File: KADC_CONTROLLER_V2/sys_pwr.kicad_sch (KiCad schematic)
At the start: 57 parts, among them J3 PJ-202AH, J6 22112022, Q1 DMN2310U-7, Q2 DMN2310U-7, U26 CSD18532Q5B, U27 MP8772GQ-Z, U28 MP8904DD-LF-Z, U29 MMSD4148T1G, U6 MP5016HGQH-Z

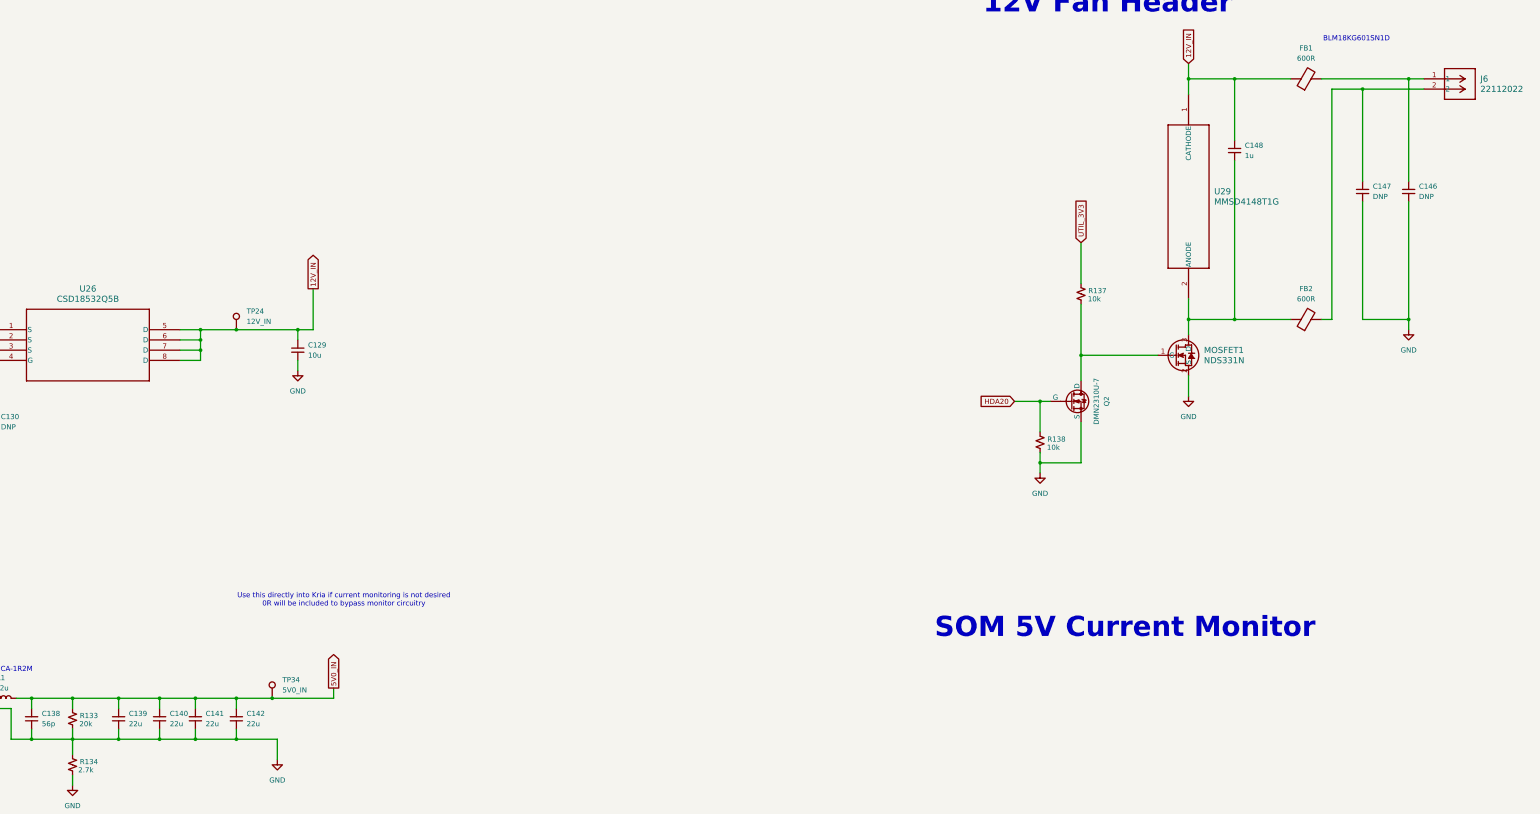
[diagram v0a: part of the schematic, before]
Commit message: Added footprints, updated schematic
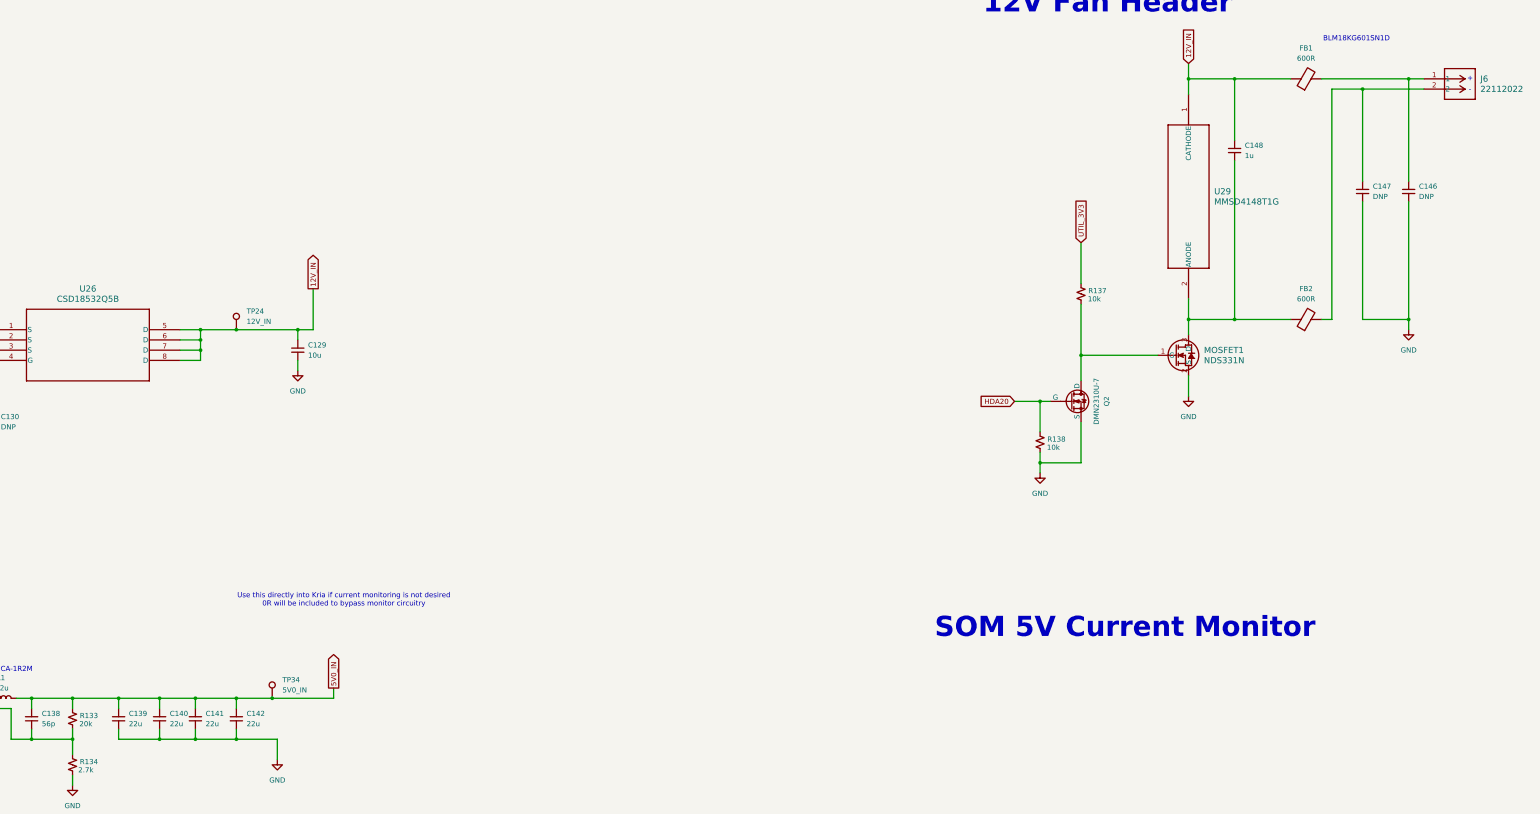
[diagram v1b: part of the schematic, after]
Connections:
- net GND: no longer C138.1, R132.1, R133.2, R134.1
- new net: C138.1, R132.1, R133.2, R134.1
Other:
- note added: "+"
- note added: "-"
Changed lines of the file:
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@@
 	(generator_version "10.0")
 	(paper "A2")
+	(text "-"
+		(exclude_from_sim no)
+		(at 558.8 47.244 0)
+		(effects
+			(font
+				(size 1.27 1.27)
+			)
+		)
+	)
 	(text "12V Plug"
 		(exclude_from_sim no)
@@
 		)
 	)
+	(text "+"
+		(exclude_from_sim no)
+		(at 558.8 44.45 0)
+		(effects
+			(font
+				(size 1.27 1.27)
+			)
+		)
+	)
 	(text "3.3 Auxiliary Regulator"
 		(exclude_from_sim no)
@@
 	)
 	(junction
-		(at 223.52 208.28)
-		(diameter 0)
-		(color 0 0 0 0)
-	)
-	(junction
 		(at 488.95 104.14)
 		(diameter 0)
@@
 		)
 		(stroke
-			(width 0)
-			(type default)
-		)
-	)
-	(wire
-		(pts
-			(xy 212.09 208.28) (xy 223.52 208.28)
-		)
-		(stroke

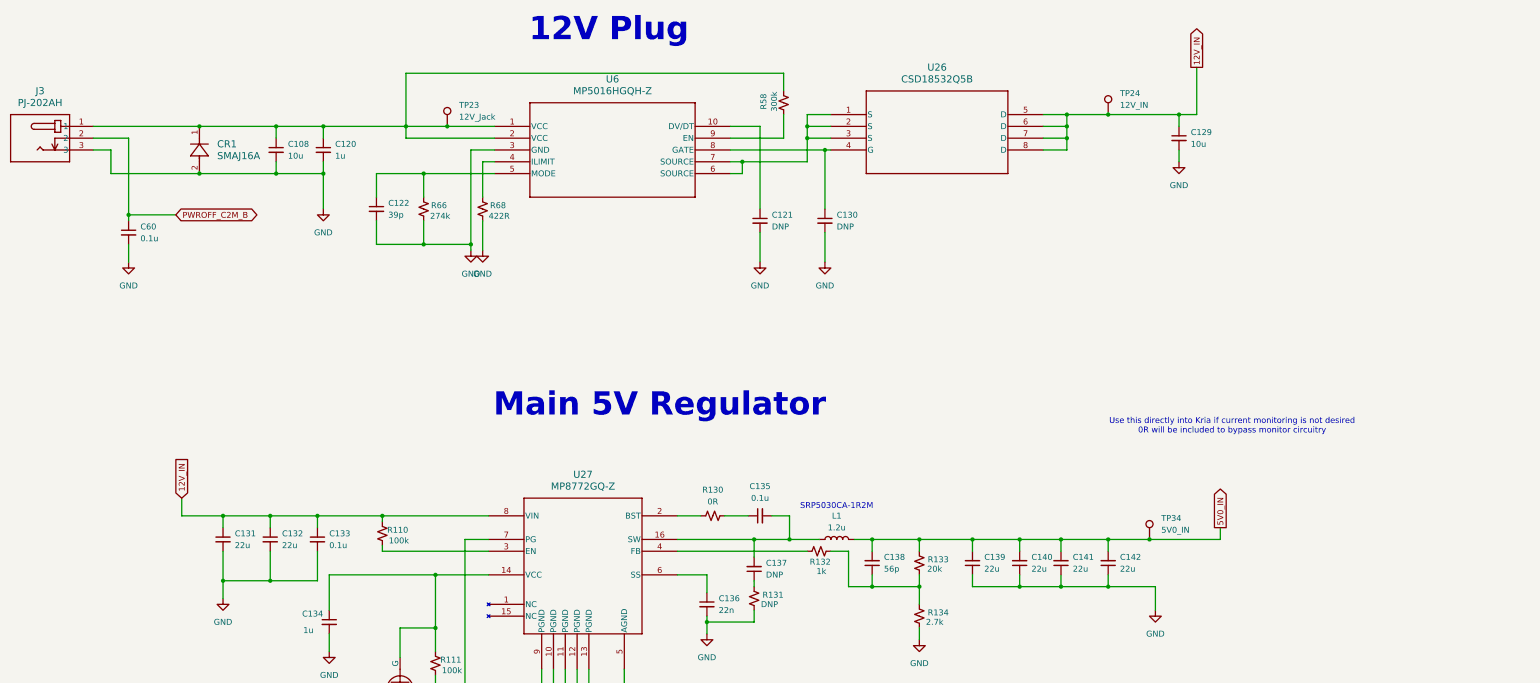
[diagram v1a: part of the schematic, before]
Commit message: Added SOM dedicated power rail
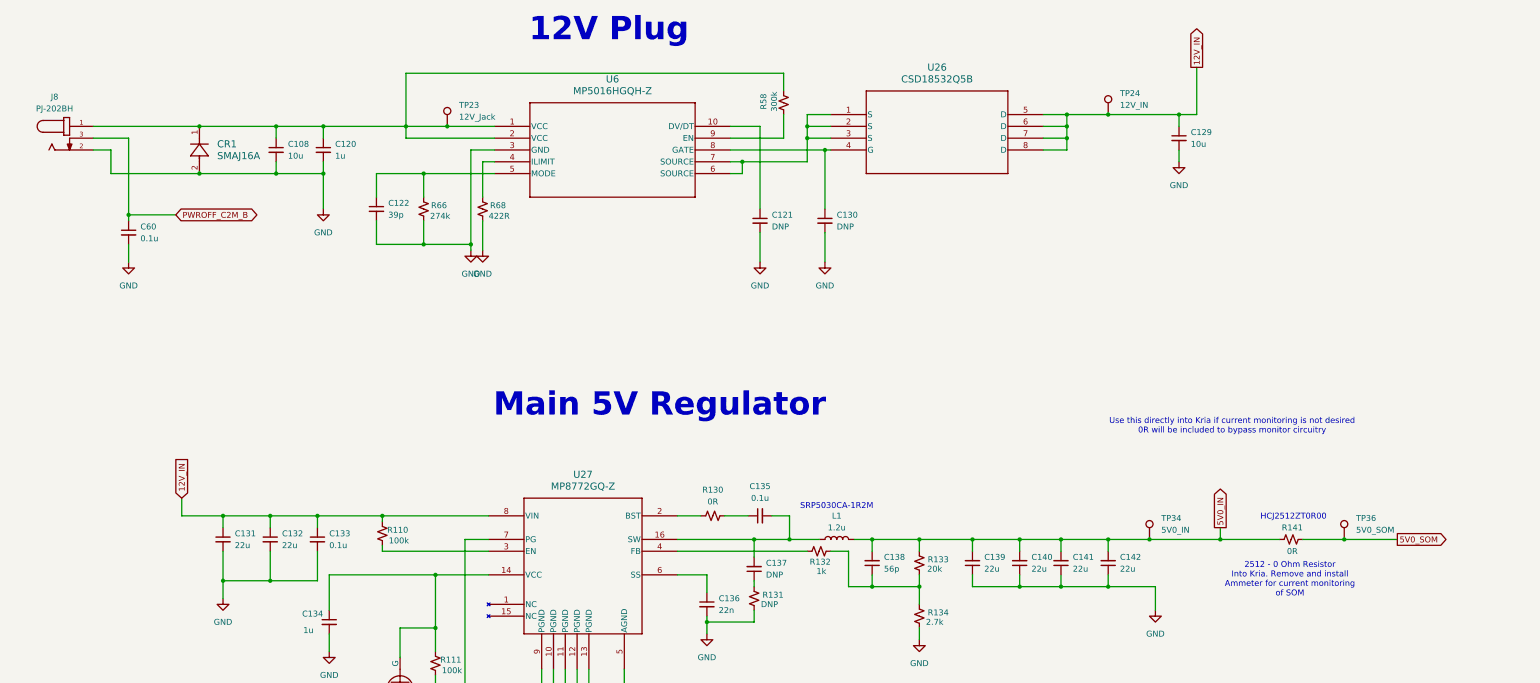
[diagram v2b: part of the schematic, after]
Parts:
- removed J3: PJ-202AH, CONN3_PJ-202_CUD, symbol PJ_202AH:PJ-202AH
- added J8: PJ-202BH, PJ-202BH:CUI_PJ-202BH, symbol PJ-202BH:PJ-202BH
- added R141: 0R, HCJ2512ZT0R00:RES_HCJ2512_STP, symbol Device:R_Small_US
- added TP36: 5V0_SOM, TestPoint:TestPoint_THTPad_1.5x1.5mm_Drill0.7mm, symbol Connector:TestPoint
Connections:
- net 5V0_IN: now also R141.1
- net GND: now also J8.2
- net PWROFF_C2M_B: now also J8.3
- net at C108.1, C120.1, CR1.1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: now also J8.1
- new net 5V0_SOM: R141.2, TP36.1
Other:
- note added: "2512 - 0 Ohm Resistor Into Kria. Remove and install Ammeter for current monitoring of SOM"
- note added: "HCJ2512ZT0R00"

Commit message: Updated Transistors
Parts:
- removed Q1: DMN2310U-7, Package_TO_SOT_SMD:TSOT-23, symbol Simulation_SPICE:NMOS
- added Q12: BSS806NEH6327XTSA1, Package_TO_SOT_SMD:SOT-23-3, symbol Transistor_FET:Q_NMOS_GSD
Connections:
- net PWROFF_C2M_B: now also Q12.3 (D)
- net at C134.1, R111.2, U27.14 (VCC): now also Q12.1 (G)
- net at R111.1, U27.7 (PG): now also Q12.2 (S)
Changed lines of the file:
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@@
 	)
 	(junction
-		(at 462.28 113.03)
+		(at 72.39 207.01)
 		(diameter 0)
 		(color 0 0 0 0)
 	)
 	(junction
-		(at 72.39 207.01)
+		(at 82.55 193.04)
 		(diameter 0)
 		(color 0 0 0 0)
 	)
 	(junction
-		(at 82.55 193.04)
+		(at 115.57 134.62)
 		(diameter 0)
 		(color 0 0 0 0)
 	)
 	(junction
-		(at 115.57 134.62)
+		(at 452.12 124.46)
 		(diameter 0)
 		(color 0 0 0 0)
@@
 	)
 	(junction
+		(at 462.28 113.03)
+		(diameter 0)
+		(color 0 0 0 0)
+	)
+	(junction
 		(at 303.53 198.12)
 		(diameter 0)
@@
 	)
 	(junction
-		(at 452.12 124.46)
-		(diameter 0)
-		(color 0 0 0 0)
-	)
-	(junction
 		(at 488.95 104.14)
 		(diameter 0)
@@
 	)
 	(symbol
-		(lib_id "Simulation_SPICE:NMOS")
-		(at 100.33 228.6 90)
-		(mirror x)
-		(unit 1)
-		(body_style 1)
-		(exclude_from_sim no)
-		(in_bom yes)
-		(on_board yes)
-		(in_pos_files yes)
-		(dnp no)
-		(property "Reference" "Q1"
-			(at 100.33 237.49 90)
-			(show_name no)
-			(do_not_autoplace no)
-			(effects
-				(font
-					(size 1.27 1.27)
-				)
-			)
-		)
-		(property "Value" "DMN2310U-7"
-			(at 100.33 234.95 90)
-			(show_name no)
-			(do_not_autoplace no)
-			(effects
-				(font
-					(size 1.27 1.27)
-				)
-			)
-		)
-		(property "Footprint" "Package_TO_SOT_SMD:TSOT-23"
-			(at 97.79 233.68 0)
-			(hide yes)
-			(show_name no)
-			(do_not_autoplace no)
-			(effects
-				(font
-					(size 1.27 1.27)
-				)
-			)
-		)
-		(property "Datasheet" "https://ngspice.sourceforge.io/docs/ngspice-html-manual/manual.xhtml#cha_MOSFETs"
-			(at 113.03 228.6 0)
-			(hide yes)
-			(show_name no)
-			(do_not_autoplace no)
-			(effects
-				(font
-					(size 1.27 1.27)
-				)
-			)
-		)
-		(property "Description" "N-MOSFET transistor, drain/source/gate"
-			(at 100.33 228.6 0)
-			(hide yes)
-			(show_name no)
-			(do_not_autoplace no)
-			(effects
-				(font
-					(size 1.27 1.27)
-				)
-			)
-		)
-		(property "Sim.Device" "NMOS"
-			(at 117.475 228.6 0)
-			(hide yes)
-			(show_name no)
-			(do_not_autoplace no)
-			(effects
-				(font
-					(size 1.27 1.27)
-				)
-			)
-		)
-		(property "Sim.Type" "VDMOS"
-			(at 119.38 228.6 0)
-			(hide yes)
-			(show_name no)
-			(do_not_autoplace no)
-			(effects
-				(font
-					(size 1.27 1.27)
-				)
-			)
-		)
-		(property "Sim.Pins" "1=D 2=G 3=S"
-			(at 115.57 228.6 0)
-			(hide yes)
-			(show_name no)
-			(do_not_autoplace no)
-			(effects
-				(font
-					(size 1.27 1.27)
-				)
-			)
-		)
-		(pin "2"
-		)
-		(pin "3"
-		)
-		(pin "1"
-		)
-		(instances
-			(project "PSEC5_Ctrl_Board"
-				(path "/165f2ae6-d522-4adf-a6c4-bb137b209d33/f466d282-efd5-4faf-90cd-789f7773e037"
-					(reference "Q1")
-					(unit 1)
-				)
-			)
-		)
-	)
-	(symbol
 		(lib_id "MP8904DD-LF-Z:MP8904DD-LF-Z")
 		(at 121.92 279.4 0)
@@
 					(unit 1)
 				)
+			)
+		)
+	)
+	(symbol
+		(lib_id "Transistor_FET:Q_NMOS_GSD")
+		(at 100.33 228.6 90)
+		(mirror x)
+		(unit 1)
+		(body_style 1)
+		(exclude_from_sim no)
+		(in_bom yes)
+		(on_board yes)
+		(in_pos_files yes)
+		(dnp no)
+		(property "Reference" "Q12"
+			(at 100.33 237.49 90)
+			(show_name no)
+			(do_not_autoplace no)
+			(effects
+				(font
+					(size 1.27 1.27)
+				)
+			)
+		)
+		(property "Value" "BSS806NEH6327XTSA1"
+			(at 100.33 234.95 90)
+			(show_name no)
+			(do_not_autoplace no)
+			(effects
+				(font
+					(size 1.27 1.27)
+				)
+			)
+		)
+		(property "Footprint" "Package_TO_SOT_SMD:SOT-23-3"
+			(at 97.79 233.68 0)
+			(hide yes)
+			(show_name no)
+			(do_not_autoplace no)
+			(effects
+				(font
+					(size 1.27 1.27)
+				)
+			)
+		)
+		(property "Datasheet" ""
+			(at 100.33 228.6 0)
+			(hide yes)
+			(show_name no)
+			(do_not_autoplace no)
+			(effects
+				(font
+					(size 1.27 1.27)
+				)
+			)
+		)
+		(property "Description" "N-MOSFET transistor, gate/source/drain"
+			(at 100.33 228.6 0)
+			(hide yes)
+			(show_name no)
+			(do_not_autoplace no)
+			(effects
+				(font
+					(size 1.27 1.27)
+				)
+			)
+		)
+		(pin "3"
+		)
+		(pin "1"
+		)
+		(pin "2"
+		)
+		(instances
+			(project "PSEC5_Ctrl_Board"
+				(path "/165f2ae6-d522-4adf-a6c4-bb137b209d33/f466d282-efd5-4faf-90cd-789f7773e037"
+					(reference "Q12")
+					(unit 1)
+				)

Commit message: Quick Updates, Power verification finalized
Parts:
- removed Q2: DMN2310U-7, Package_TO_SOT_SMD:TSOT-23, symbol Simulation_SPICE:NMOS
- added C153, C154: 47u, Capacitor_SMD:C_0603_1608Metric, symbol Device:C_Small
- added C247: 1u, Capacitor_SMD:C_0603_1608Metric, symbol Device:C_Small
- added C248: 0.1u, Capacitor_SMD:C_0603_1608Metric, symbol Device:C_Small
- added Q13: BSS806NEH6327XTSA1, Package_TO_SOT_SMD:SOT-23-3, symbol Transistor_FET:Q_NMOS_GSD
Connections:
- net 5V0_SOM: now also C153.2, C154.2, C247.2, C248.2
- net GND: now also C153.1, C154.1, C247.1, C248.1, Q13.2 (S)
- net HDA20: now also Q13.1 (G)
- net at MOSFET1.1 (G), R137.2: now also Q13.3 (D)

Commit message: Reupdate for verify
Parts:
- J6: footprint CONN_A-6373-02A_MOL -> 22112022:CONN_A-6373-02A_MOL
- L1: footprint (none) -> Inductor_SMD:L_Bourns_SRP5030T
- U26: footprint DNK8 -> CSD18532Q5B:DNK8
- U27: footprint QFN-16_MP8772GQ-P_MNP -> MP8772GQ_Z:QFN-16_MP8772GQ-P_MNP
- U28: footprint QFN8_MNP -> MP8904DD_LF_Z:QFN8_MNP
- U29: footprint SOD-123_ONS -> MMSD4148T1G:SOD-123_ONS
- U6: footprint QFN-10_MP5016H_MNP -> MP5016HGQH_Z:QFN-10_MP5016H_MNP
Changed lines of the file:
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@@
 			)
 		)
-		(property "Footprint" "QFN8_MNP"
+		(property "Footprint" "MP8904DD_LF_Z:QFN8_MNP"
 			(at 135.382 262.636 0)
 			(hide yes)
@@
 			)
 		)
-		(property "Footprint" "CONN_A-6373-02A_MOL"
+		(property "Footprint" "22112022:CONN_A-6373-02A_MOL"
 			(at 547.37 44.45 0)
 			(hide yes)
@@
 			)
 		)
-		(property "Footprint" "QFN-10_MP5016H_MNP"
+		(property "Footprint" "MP5016HGQH_Z:QFN-10_MP5016H_MNP"
 			(at 120.65 109.22 0)
 			(hide yes)
@@
 			)
 		)
-		(property "Footprint" ""
+		(property "Footprint" "Inductor_SMD:L_Bourns_SRP5030T"
 			(at 194.31 198.12 0)
 			(hide yes)
@@
 			)
 		)
-		(property "Footprint" "SOD-123_ONS"
+		(property "Footprint" "MMSD4148T1G:SOD-123_ONS"
 			(at 488.95 48.26 0)
 			(hide yes)
@@
 			)
 		)
-		(property "Footprint" "DNK8"
+		(property "Footprint" "CSD18532Q5B:DNK8"
 			(at 193.04 106.68 0)
 			(hide yes)
@@
 			)
 		)
-		(property "Footprint" "QFN-16_MP8772GQ-P_MNP"
+		(property "Footprint" "MP8772GQ_Z:QFN-16_MP8772GQ-P_MNP"
 			(at 139.446 178.562 0)
 			(hide yes)

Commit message: update for verification
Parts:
- added TP37: PWROFF_C2M_B, TestPoint:TestPoint_THTPad_1.5x1.5mm_Drill0.7mm, symbol Connector:TestPoint
- added TP40: GND, TestPoint:TestPoint_THTPad_1.5x1.5mm_Drill0.7mm, symbol Connector:TestPoint
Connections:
- net GND: now also TP40.1
- net PWROFF_C2M_B: now also TP37.1
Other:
- note added: "Keep TP40 near PWROFF As manual ground to pull low"

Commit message: update
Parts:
- CR1: footprint DO214AC_LTF -> SMAJ16A:DO214AC_LTF
- J8: footprint PJ-202BH:CUI_PJ-202BH -> PJ_202AH:CONN3_PJ-202_CUD
- MOSFET1: footprint SOT23_527AG_ONS -> NDS331N:SOT23_527AG_ONS
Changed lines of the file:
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@@
 			)
 		)
-		(property "Footprint" "DO214AC_LTF"
+		(property "Footprint" "SMAJ16A:DO214AC_LTF"
 			(at 57.15 119.38 0)
 			(hide yes)
@@
 			)
 		)
-		(property "Footprint" "PJ-202BH:CUI_PJ-202BH"
+		(property "Footprint" "PJ_202AH:CONN3_PJ-202_CUD"
 			(at 34.798 99.568 0)
 			(hide yes)
@@
 			)
 		)
-		(property "Footprint" "SOT23_527AG_ONS"
+		(property "Footprint" "NDS331N:SOT23_527AG_ONS"
 			(at 481.33 113.03 0)
 			(hide yes)
